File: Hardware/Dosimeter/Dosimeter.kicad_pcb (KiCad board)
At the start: 2 copper layers, 92 x 70 mm, 43 parts, among them J1 USB_B_Mini, J2 Vin +12, J3 Conn_01x01_Female, J4 Conn_01x01_Female, J5 Conn_01x02_Male, J6 Conn_01x02_Male, J7 Conn_01x01_Female, Q1 BC846, SW1 SW_Push, SW2 SW_Push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

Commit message: complete HW, add Software
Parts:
- added BT1: Battery, MK_Footprints:BatteryHolder_Keystone_2477_4xAA, B.Cu at (84.0, 95.0)
- added J8: Conn_01x04_Male, Connector_PinHeader_2.54mm:PinHeader_1x04_P2.54mm_Vertical, F.Cu at (83.4, 115.7)
- C10: value 47p -> 100p; footprint Capacitor_THT:C_Disc_D8.0mm_W5.0mm_P10.00mm -> Capacitor_THT:C_Axial_L3.8mm_D2.6mm_P12.50mm_Horizontal
- moved R13 60.9 mm to (92.2, 117.9), turned to 90 degrees
- moved Q1 53.7 mm to (92.2, 101.1), turned to 270 degrees
- moved C8 53.6 mm to (75.4, 96.8), turned to 90 degrees
- moved C6 34.7 mm to (103.5, 108.6), turned to 90 degrees
- moved C5 26.0 mm to (106.9, 96.8)
- moved C9 24.6 mm to (109.1, 108.7), turned to 270 degrees
- moved C11 9.12 mm to (78.9, 107.4), turned to 0 degrees
- moved J5 8.43 mm to (75.1, 73.2)
- moved J6 8.43 mm to (75.1, 84.8)
- moved SW1 8.43 mm to (81.1, 74.8)
- moved SW2 8.43 mm to (81.1, 85.8)
- moved D4 5.57 mm to (80.3, 128.7), turned to 0 degrees
- moved U3 5.32 mm to (106.3, 109.1), turned to 90 degrees
- moved D1 4.51 mm to (105.3, 114.8), turned to 270 degrees
- moved R1 2.17 mm to (106.9, 114.8), turned to 90 degrees
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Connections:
- RV1 pad 3: Net-(R10-Pad1) -> +6V
- U2 pad 23: (no net) -> SWDIO
- U2 pad 24: (no net) -> SWCLK
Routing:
- net +6V: track 1.67 -> 143.3 mm, vias 1 -> 5
- net +3V3: track 77.6 -> 178.0 mm, vias 0 -> 5
- net GND: track 135.3 -> 192.6 mm, vias 1 -> 5
- net /D+: track 0.00 -> 44.9 mm, vias 0 -> 2
- net /D-: track 0.00 -> 42.9 mm, vias 0 -> 2
- net /DB3: track 0.00 -> 29.0 mm
- net /DB0: track 0.00 -> 28.8 mm
- net /DB1: track 0.00 -> 27.2 mm
- net /DB2: track 0.00 -> 27.1 mm
- net SWCLK: track 0.00 -> 23.5 mm
- net SWDIO: track 0.00 -> 21.4 mm
- net +5V: track 0.00 -> 9.06 mm
- net Net-(J5-Pad1): track 51.9 -> 44.3 mm
- net Net-(J6-Pad1): track 42.7 -> 36.3 mm
- net Net-(C5-Pad1): track 0.00 -> 4.56 mm
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
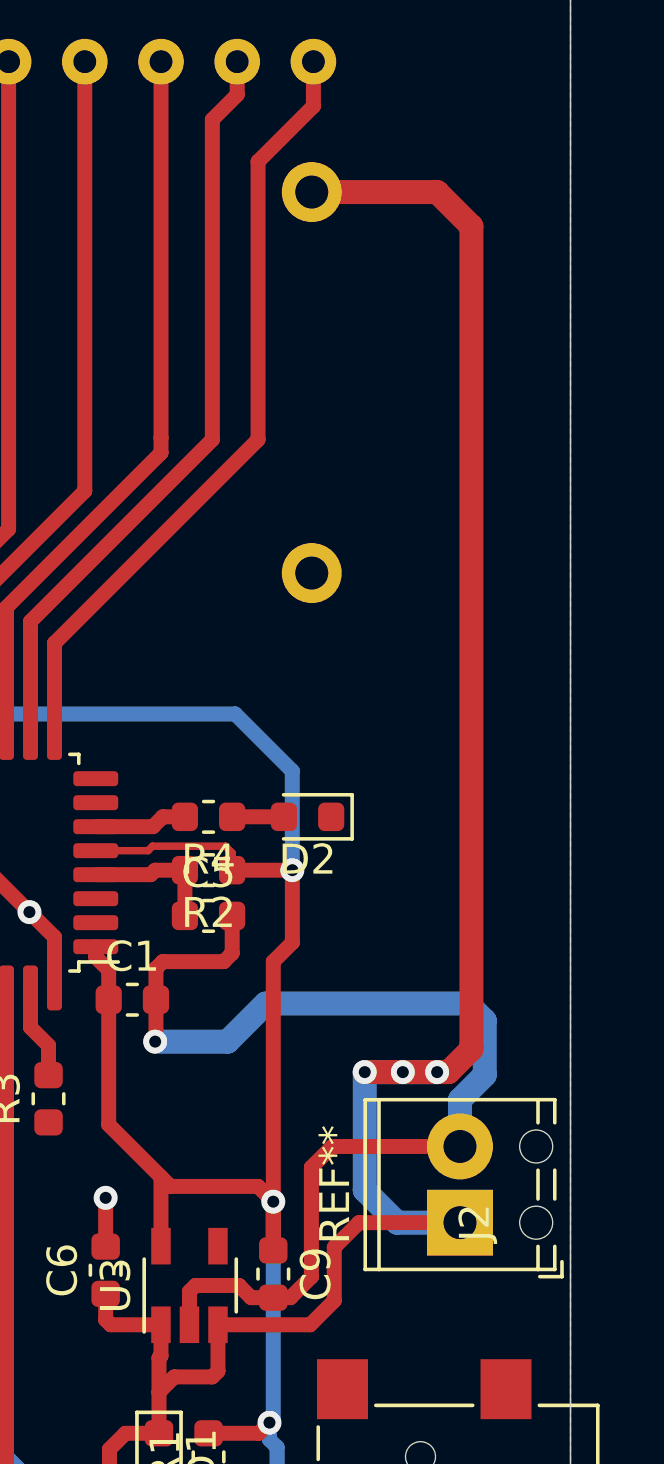
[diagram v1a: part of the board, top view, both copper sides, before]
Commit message: update hardware (add switch)
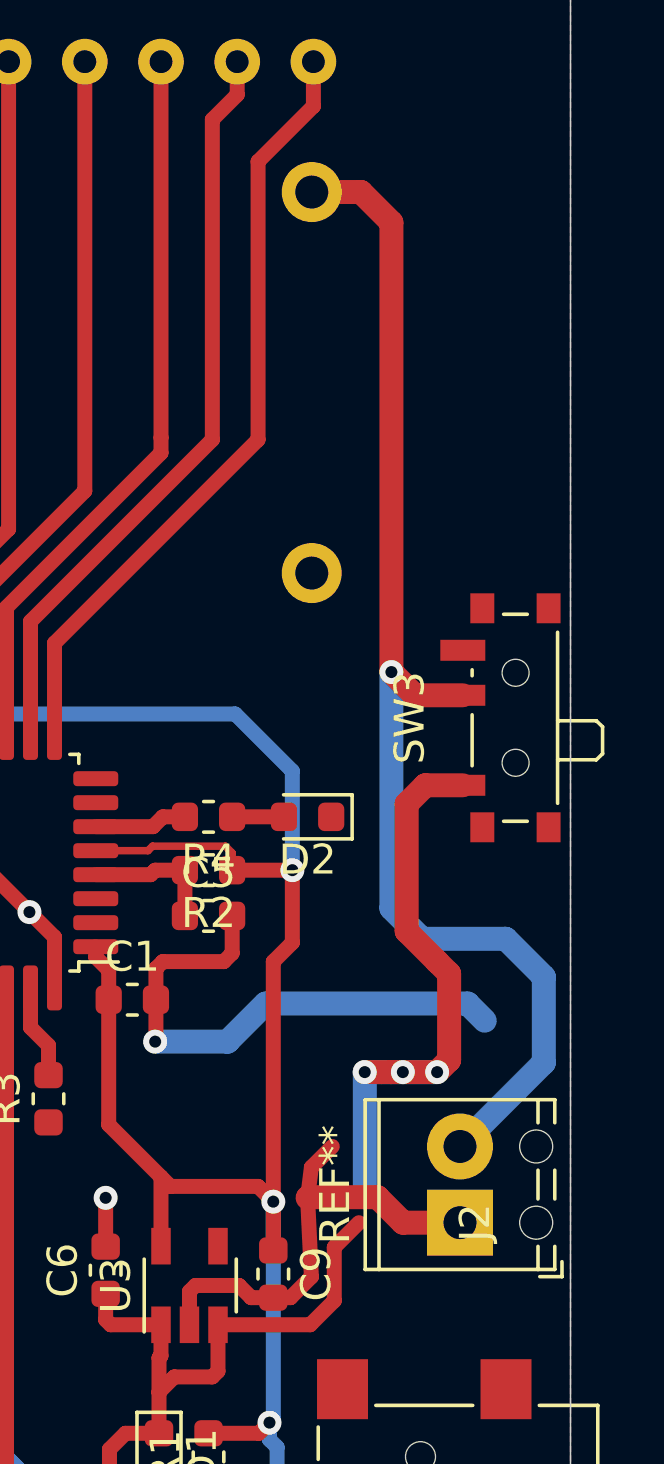
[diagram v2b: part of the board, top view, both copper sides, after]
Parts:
- added SW3: SW_SPST, Button_Switch_SMD:SW_SPDT_PCM12, F.Cu at (116.8, 90.2)
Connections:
- BT1 pad 1: +6V -> Net-(BT1-Pad1)
- J1 pad 4: (no net) -> Net-(J1-Pad4)
- J2 pad 1: +6V -> GND
- J2 pad 2: GND -> Net-(BT1-Pad1)
- U2 pad 2: (no net) -> Net-(U2-Pad2)
- U2 pad 26: (no net) -> Net-(U2-Pad26)
- U2 pad 3: (no net) -> Net-(U2-Pad3)
- U2 pad 7: (no net) -> Net-(U2-Pad7)
- U2 pad 8: (no net) -> Net-(U2-Pad8)
- U3 pad 4: (no net) -> Net-(U3-Pad4)
- U4 pad 5: (no net) -> Net-(U4-Pad5)
- U5 pad 5: (no net) -> Net-(U5-Pad5)
- U6 pad 15: (no net) -> Net-(U6-Pad15)
- U6 pad 16: (no net) -> Net-(U6-Pad16)
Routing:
- net Net-(BT1-Pad1): track 0.00 -> 41.0 mm, vias 0 -> 1
- net +6V: track 143.3 -> 110.5 mm
- net GND: track 192.6 -> 189.3 mm
